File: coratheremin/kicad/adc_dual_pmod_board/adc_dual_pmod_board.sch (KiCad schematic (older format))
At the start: 63 parts, among them J1 PITCH, J2 VOLUME, J3 PMOD_A, J4 PMOD_B, J5 AUX1, U1 LP2985-4.5, U2 LP2985-4.5, U3 LP2985-3.3, U4 LP2985-3.3, U5 AD9283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

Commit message: update PCBs
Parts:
- U5, U6: footprint Package_SO:SSOP-20_4.4x6.5mm_P0.65mm -> Package_SO:SSOP-20_5.3x7.2mm_P0.65mm
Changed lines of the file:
@@
 F 0 "U5" H 8900 4300 50  0000 C CNN
 F 1 "AD9283" H 8900 2850 50  0000 C CNN
-F 2 "Package_SO:SSOP-20_4.4x6.5mm_P0.65mm" H 8550 3550 50  0001 C CNN
+F 2 "Package_SO:SSOP-20_5.3x7.2mm_P0.65mm" H 8550 3550 50  0001 C CNN
 F 3 "https://www.analog.com/media/en/technical-documentation/data-sheets/AD9283.pdf" H 8550 3550 50  0001 C CNN
 	1    8550 3550
@@
 F 0 "U6" H 8900 8850 50  0000 C CNN
 F 1 "AD9283" H 8900 7400 50  0000 C CNN
-F 2 "Package_SO:SSOP-20_4.4x6.5mm_P0.65mm" H 8550 8100 50  0001 C CNN
+F 2 "Package_SO:SSOP-20_5.3x7.2mm_P0.65mm" H 8550 8100 50  0001 C CNN
 F 3 "https://www.analog.com/media/en/technical-documentation/data-sheets/AD9283.pdf" H 8550 8100 50  0001 C CNN
 	1    8550 8100

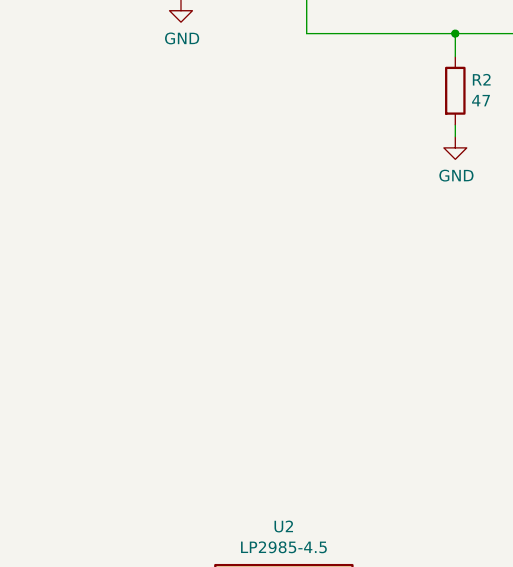
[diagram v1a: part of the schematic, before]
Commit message: cora z7 theremin dual 100MHz ADC pmods board
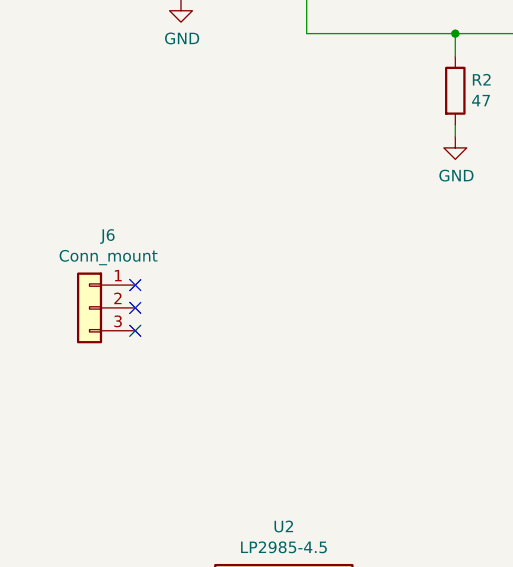
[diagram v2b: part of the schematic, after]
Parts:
- added J6: Conn_mount, Connector_PinSocket_2.54mm:PinSocket_1x03_P2.54mm_Vertical, symbol Connector_Generic:Conn_01x03
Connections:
- no-connect marks 3 -> 6
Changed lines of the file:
@@
 Sheet 1 1
 Title "ADC dual PMOD board for Digital Theremin"
-Date "2020-10-31"
+Date "2020-11-10"
 Rev "0.1"
 Comp "Vadim Lopatin"
@@
 Wire Bus Line
 	9950 7500 11800 7500
+Connection ~ 11800 7500
+$Comp
+L Connector_Generic:Conn_01x03 J6
+U 1 1 5FB3BB5E
+P 1550 5250
+F 0 "J6" H 1468 5567 50  0000 C CNN
+F 1 "Conn_mount" H 1468 5476 50  0000 C CNN
+F 2 "Connector_PinSocket_2.54mm:PinSocket_1x03_P2.54mm_Vertical" H 1550 5250 50  0001 C CNN
+F 3 "~" H 1550 5250 50  0001 C CNN
+	1    1550 5250
+	-1   0    0    -1
+$EndComp
+NoConn ~ 1750 5350
+NoConn ~ 1750 5250
+NoConn ~ 1750 5150
 Wire Bus Line
 	9950 2900 11800 2900
 Wire Bus Line
+	11800 7500 11800 8450
+Wire Bus Line
 	11800 2900 11800 7500
-Wire Bus Line
-	11800 7500 11800 8450
 Wire Bus Line
 	9950 2900 9950 4100
 Wire Bus Line
 	9950 7500 9950 8650
-Connection ~ 11800 7500
 $EndSCHEMATC

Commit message: update ADC board pcb, replace ssop20 footprint
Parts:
- U5, U6: footprint Package_SO:SSOP-20_5.3x7.2mm_P0.65mm -> ssop-20_custom:SSOP-20-wide-7-P0.65
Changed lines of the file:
@@
 F 0 "U5" H 8900 4300 50  0000 C CNN
 F 1 "AD9283" H 8900 2850 50  0000 C CNN
-F 2 "Package_SO:SSOP-20_5.3x7.2mm_P0.65mm" H 8550 3550 50  0001 C CNN
+F 2 "ssop-20_custom:SSOP-20-wide-7-P0.65" H 8550 3550 50  0001 C CNN
 F 3 "https://www.analog.com/media/en/technical-documentation/data-sheets/AD9283.pdf" H 8550 3550 50  0001 C CNN
 	1    8550 3550
@@
 F 0 "U6" H 8900 8850 50  0000 C CNN
 F 1 "AD9283" H 8900 7400 50  0000 C CNN
-F 2 "Package_SO:SSOP-20_5.3x7.2mm_P0.65mm" H 8550 8100 50  0001 C CNN
+F 2 "ssop-20_custom:SSOP-20-wide-7-P0.65" H 8550 8100 50  0001 C CNN
 F 3 "https://www.analog.com/media/en/technical-documentation/data-sheets/AD9283.pdf" H 8550 8100 50  0001 C CNN
 	1    8550 8100
